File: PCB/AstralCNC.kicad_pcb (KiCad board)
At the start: 2 copper layers, 60 x 54 mm, 47 parts, among them J11 Conn_01x02, J31 Conn_01x10_Pin, J310 Conn_02x04_Counter_Clockwise, J311 Conn_01x04_Pin, J312 Conn_01x04_Pin, J313 Conn_01x04_Pin, J32 Conn_01x04_Pin, J33 Conn_01x03_Pin, J34 Conn_01x03_Pin, J35 Conn_01x03_Pin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

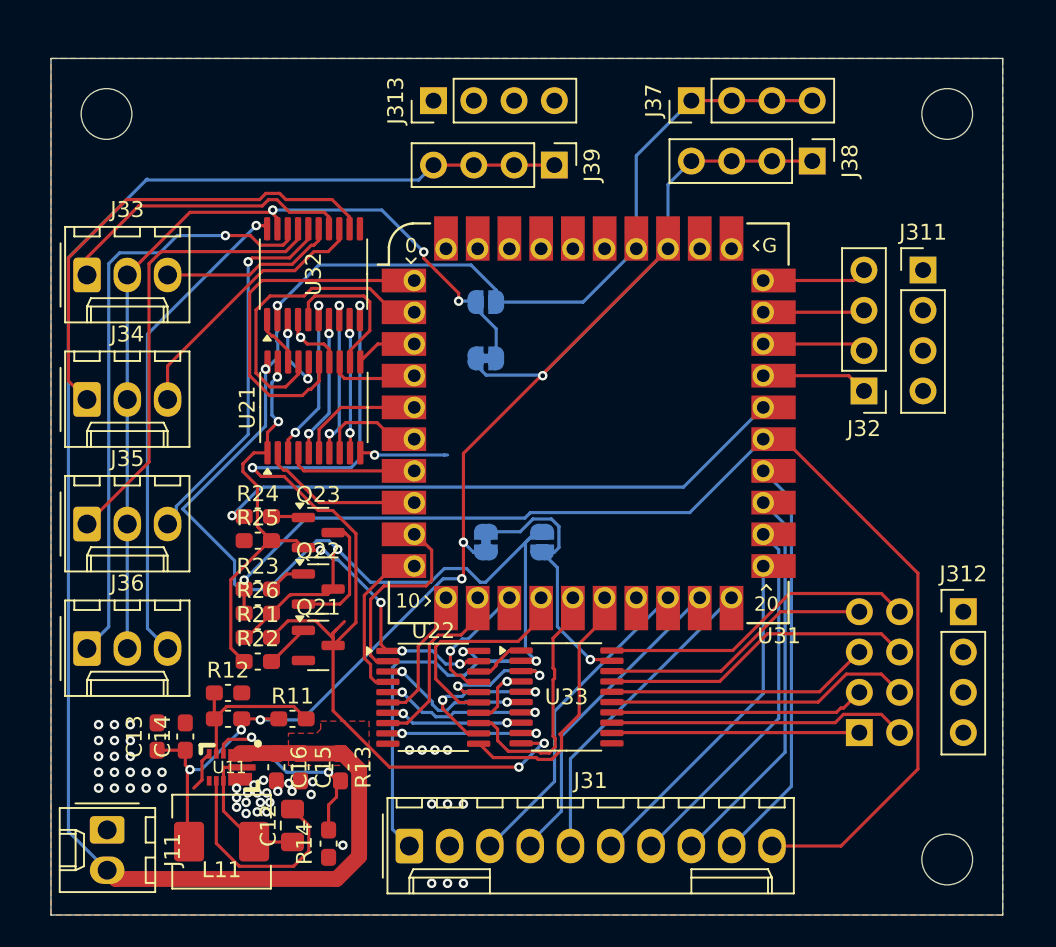
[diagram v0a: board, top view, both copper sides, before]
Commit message: Update journal entries: Adjusted hours for June 17 and June 19, added USB-C connector details, and included an image for clarity.
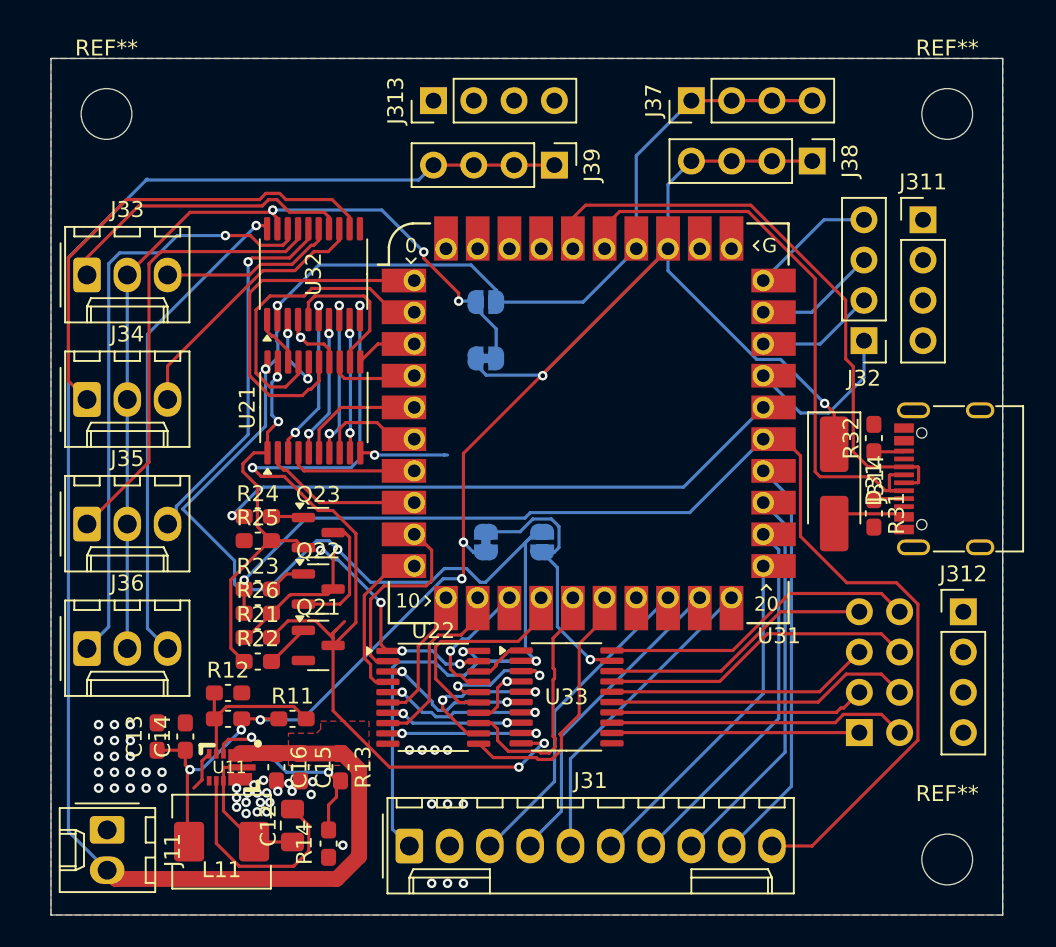
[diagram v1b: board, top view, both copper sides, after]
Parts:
- added D31: D_Shockley, Diode_SMD:D_SMA_Handsoldering, F.Cu at (175.4, 97.8)
- added J314: USB_C_Receptacle_USB2.0_16P, Connector_USB:USB_C_Receptacle_G-Switch_GT-USB-7010ASV, F.Cu at (183.5, 97.5)
- added R31: R, Capacitor_SMD:C_0603_1608Metric_Pad1.08x0.95mm_HandSolder, F.Cu at (177.9, 99.7)
- added R32: R, Capacitor_SMD:C_0603_1608Metric_Pad1.08x0.95mm_HandSolder, F.Cu at (177.9, 94.9)
- moved J311 3.17 mm to (181.0, 81.2)
- moved J32 3.17 mm to (177.2, 88.8)
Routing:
- net D+: track 0.00 -> 38.1 mm
- net D-: track 0.00 -> 37.9 mm
- net +5V: track 89.3 -> 106.9 mm, vias 6 -> 7
- net Net-(D31-A): track 0.00 -> 4.73 mm
- net A1: track 6.10 -> 10.6 mm
- net A3: track 5.75 -> 7.71 mm
- net A4: track 5.97 -> 7.94 mm
- net Net-(J314-CC1): track 0.00 -> 1.93 mm
- net Net-(J314-CC2): track 0.00 -> 1.92 mm
- net A2: track 5.87 -> 7.49 mm
- net E_STOP: track 74.7 -> 76.1 mm

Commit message: bruh
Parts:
- added D1: LED, Connector_PinHeader_2.54mm:PinHeader_1x02_P2.54mm_Vertical, F.Cu at (167.8, 115.5)
- added R1: R, Capacitor_SMD:C_0603_1608Metric_Pad1.08x0.95mm_HandSolder, F.Cu at (172.1, 115.5)
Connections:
- J31 pad 3: AUX3 -> AUX_4
- J31 pad 4: AUX2 -> AUX3
- J31 pad 5: AUX1 -> AUX2
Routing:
- net X_ENDSTOP: track 25.9 -> 0.00 mm
- net AUX_4: track 0.00 -> 19.5 mm
- net AUX1: track 19.9 -> 12.0 mm
- net Net-(D1-K): track 0.00 -> 3.46 mm
- net ENABLE_HIGH: track 61.3 -> 59.7 mm
- net AUX3: track 20.3 -> 19.2 mm
- net AUX2: track 20.1 -> 19.0 mm
- net W_ENDSTOP: track 21.6 -> 22.4 mm
- net GND: track 8.12 -> 8.77 mm, vias 50 -> 65
- net Z_ENDSTOP: track 23.4 -> 24.0 mm
- net Net-(U22-1Y2): vias 1 -> 0
- net Net-(U21-1Y2): vias 1 -> 0
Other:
- board text added: "10"
- board text added: "11"
- board text added: "12"
- board text added: "12v"
- board text added: "13"
- board text added: "14"
- board text added: "15"
- board text added: "16"
- board text added: "17"
- board text added: "18"
- board text added: "19"
- board text added: "20"
- board text added: "21"
- board text added: "22"
- board text added: "23"
- board text added: "24"
- board text added: "3.3v"
- board text added: "5v"
- board text added: "A1"
- board text added: "A4"
- board text added: "DIR"
- board text added: "E-Stop"
- board text added: "GND"
- board text added: "GP0"
- board text added: "GP1"
- board text added: "GP6"
- board text added: "GP7"
- board text added: "GP8"
- board text added: "GP9"
- board text added: "STEP"
- board text added: "VCCB"

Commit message: Added pull downs for safety
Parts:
- added R10: 10k, Capacitor_SMD:C_0603_1608Metric_Pad1.08x0.95mm_HandSolder, F.Cu at (175.5, 115.5)
- added R15: 10k, Capacitor_SMD:C_0603_1608Metric_Pad1.08x0.95mm_HandSolder, F.Cu at (179.0, 115.5)
- added R16: 10k, Capacitor_SMD:C_0603_1608Metric_Pad1.08x0.95mm_HandSolder, F.Cu at (179.0, 117.2)
- added R17: 10k, Capacitor_SMD:C_0603_1608Metric_Pad1.08x0.95mm_HandSolder, F.Cu at (183.5, 116.0)
- added R18: 10k, Capacitor_SMD:C_0603_1608Metric_Pad1.08x0.95mm_HandSolder, F.Cu at (172.0, 110.0)
- added R19: 10k, Capacitor_SMD:C_0603_1608Metric_Pad1.08x0.95mm_HandSolder, F.Cu at (172.0, 108.5)
- added R2: 10k, Capacitor_SMD:C_0603_1608Metric_Pad1.08x0.95mm_HandSolder, F.Cu at (134.8, 79.0)
- added R20: 10k, Capacitor_SMD:C_0603_1608Metric_Pad1.08x0.95mm_HandSolder, F.Cu at (177.0, 103.2)
- added R27: 10k, Capacitor_SMD:C_0603_1608Metric_Pad1.08x0.95mm_HandSolder, F.Cu at (136.5, 100.8)
- added R28: 10k, Capacitor_SMD:C_0603_1608Metric_Pad1.08x0.95mm_HandSolder, F.Cu at (174.5, 102.8)
- added R3: 10k, Capacitor_SMD:C_0603_1608Metric_Pad1.08x0.95mm_HandSolder, F.Cu at (137.0, 91.8)
- added R4: 10k, Capacitor_SMD:C_0603_1608Metric_Pad1.08x0.95mm_HandSolder, F.Cu at (136.0, 105.5)
- added R5: 10k, Capacitor_SMD:C_0603_1608Metric_Pad1.08x0.95mm_HandSolder, F.Cu at (143.5, 78.5)
- added R6: 10k, Capacitor_SMD:C_0603_1608Metric_Pad1.08x0.95mm_HandSolder, F.Cu at (137.1, 81.6)
- added R7: 10k, Capacitor_SMD:C_0603_1608Metric_Pad1.08x0.95mm_HandSolder, F.Cu at (136.2, 94.5)
- added R8: 10k, Capacitor_SMD:C_0603_1608Metric_Pad1.08x0.95mm_HandSolder, F.Cu at (127.2, 113.2)
- added R9: 10k, Capacitor_SMD:C_0603_1608Metric_Pad1.08x0.95mm_HandSolder, F.Cu at (128.8, 113.2)
- moved J314 1.43 mm to (183.5, 96.1)
- moved R31 1.43 mm to (177.9, 98.3)
- moved R32 1.43 mm to (177.9, 93.5)
- moved D31 1.43 mm to (175.4, 96.4)
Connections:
- U21 pad 11: Y_STEP_3.3 -> Z_STEP_3.3
- U21 pad 13: Y_DIR_3.3 -> X_DIR_3.3
- U21 pad 15: Z_STEP_3.3 -> X_STEP_3.3
- U21 pad 17: Z_DIR_3.3 -> Y_STEP_3.3
- U21 pad 6: X_STEP_3.3 -> Y_DIR_3.3
- U21 pad 8: X_DIR_3.3 -> Z_DIR_3.3
- U31 pad 1: Z_STEP_3.3 -> X_STEP_3.3
- U31 pad 2: Z_DIR_3.3 -> Y_STEP_3.3
- U31 pad 3: Y_STEP_3.3 -> Z_STEP_3.3
- U31 pad 4: Y_DIR_3.3 -> X_DIR_3.3
- U31 pad 5: X_STEP_3.3 -> Y_DIR_3.3
- U31 pad 6: X_DIR_3.3 -> Z_DIR_3.3
- U32 pad 12: Y_STEP -> Z_STEP
- U32 pad 13: Y_DIR -> X_DIR
- U32 pad 14: Z_STEP -> X_STEP
- U32 pad 15: Z_DIR -> Y_STEP
- U32 pad 16: X_DIR -> Z_DIR
- U32 pad 17: X_STEP -> Y_DIR
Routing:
- net X_ENDSTOP: track 0.00 -> 25.9 mm
- net GND: track 8.77 -> 27.9 mm, vias 65 -> 82
- net Y_STEP_3.3: track 3.21 -> 20.5 mm
- net Z_STEP_3.3: track 21.8 -> 4.52 mm
- net X_STEP_3.3: track 7.44 -> 21.1 mm
- net Z_DIR_3.3: track 19.3 -> 6.73 mm
- net E_STOP: track 76.1 -> 66.4 mm
- net X_STEP: track 28.7 -> 38.4 mm
- net AUX_G: track 16.1 -> 25.3 mm
- net AUX_C: track 17.1 -> 26.2 mm
- net Net-(D31-A): track 4.73 -> 11.5 mm
- net Y_STEP: track 30.2 -> 23.6 mm, vias 0 -> 2
- net AUX_F: track 19.3 -> 25.7 mm
- net AUX_A: track 30.8 -> 36.5 mm
- net +5V: track 106.7 -> 111.5 mm, vias 7 -> 6
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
